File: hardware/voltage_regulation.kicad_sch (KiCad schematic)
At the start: 33 parts, among them U4 TPS51388VABR, U5 LD39050PU33R

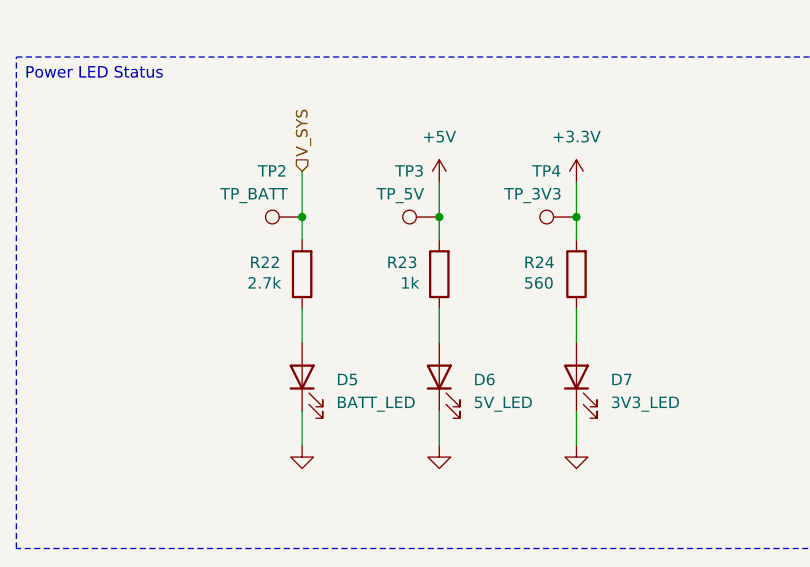
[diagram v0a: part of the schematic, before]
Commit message: Adding MPN to parts
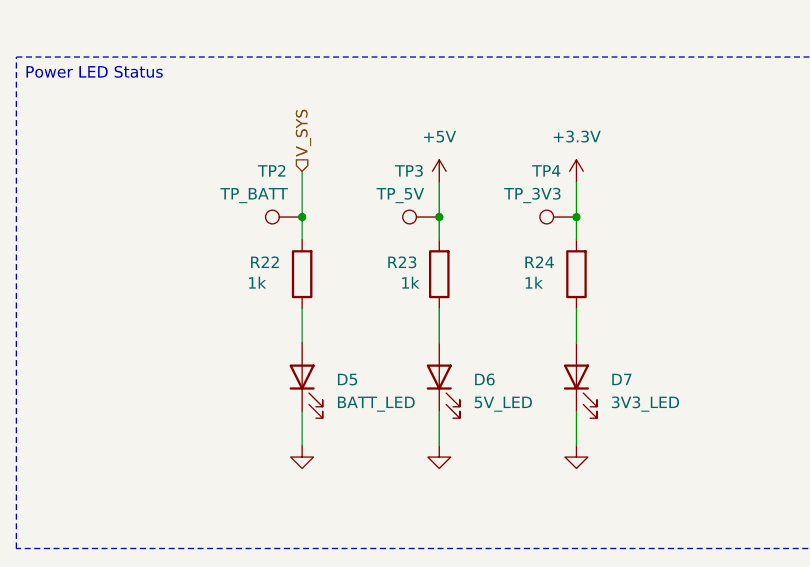
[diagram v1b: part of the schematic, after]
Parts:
- C18, C19: JLCPCB Part# (none) -> C49326357; MPN (none) -> 0603X5R105K160NT
- R15, R19: JLCPCB Part# (none) -> C844916; MPN (none) -> CRCW0603100KFKEA
- R17: JLCPCB Part# (none) -> C844135
- R21: JLCPCB Part# (none) -> C844803; MPN (none) -> CRCW060368K0FKEA
- R22: value 2.7k -> 1k; footprint Resistor_SMD:R_0402_1005Metric -> Resistor_SMD:R_0603_1608Metric; MPN (none) -> CRCW06031K00JNEAC
- R23: footprint Resistor_SMD:R_0402_1005Metric -> Resistor_SMD:R_0603_1608Metric; JLCPCB Part# (none) -> C844135; MPN (none) -> CRCW06031K00JNEAC
- R24: value 560 -> 1k; footprint Resistor_SMD:R_0402_1005Metric -> Resistor_SMD:R_0603_1608Metric; JLCPCB Part# (none) -> C844135; MPN (none) -> CRCW06031K00JNEAC
- TP2, TP3, TP4: now left out of the parts list

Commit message: Replacing components
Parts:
- C13, C14, C15, C16: JLCPCB Part# C49326685 -> C45783; MPN 0805X5R226M100NT -> CL21A226MAQNNNE
- C18, C19: JLCPCB Part# C49326357 -> C15849; MPN 0603X5R105K160NT -> CL10A105KB8NNNC
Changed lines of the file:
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@@
 			)
 		)
-		(property "MPN" "0805X5R226M100NT"
+		(property "MPN" "CL21A226MAQNNNE"
 			(at 209.55 53.34 0)
 			(hide yes)
@@
 			)
 		)
-		(property "JLCPCB Part#" "C49326685"
+		(property "JLCPCB Part#" "C45783"
 			(at 209.55 53.34 0)
 			(hide yes)
@@
 			)
 		)
-		(property "MPN" "0603X5R105K160NT"
+		(property "MPN" "CL10A105KB8NNNC"
 			(at 177.8 132.08 0)
 			(hide yes)
@@
 			)
 		)
-		(property "JLCPCB Part#" "C49326357"
+		(property "JLCPCB Part#" "C15849"
 			(at 177.8 132.08 0)
 			(hide yes)
@@
 			)
 		)
-		(property "v" ""
-			(at 111.76 139.7 90)
-			(hide yes)
-			(show_name no)
-			(do_not_autoplace no)
-			(effects
-				(font
-					(size 1.27 1.27)
-				)
-			)
-		)
 		(pin "2"
 		)
@@
 			)
 		)
-		(property "v" ""
-			(at 96.52 139.7 90)
-			(hide yes)
-			(show_name no)
-			(do_not_autoplace no)
-			(effects
-				(font
-					(size 1.27 1.27)
-				)
-			)
-		)
 		(pin "2"
 		)
@@
 			)
 		)
-		(property "MPN" "0603X5R105K160NT"
+		(property "MPN" "CL10A105KB8NNNC"
 			(at 223.52 132.08 0)
 			(hide yes)
@@
 			)
 		)
-		(property "JLCPCB Part#" "C49326357"
+		(property "JLCPCB Part#" "C15849"
 			(at 223.52 132.08 0)
 			(hide yes)
@@
 			)
 		)
-		(property "MPN" "0805X5R226M100NT"
+		(property "MPN" "CL21A226MAQNNNE"
 			(at 217.17 53.34 0)
 			(hide yes)
@@
 			)
 		)
-		(property "JLCPCB Part#" "C49326685"
+		(property "JLCPCB Part#" "C45783"
 			(at 217.17 53.34 0)
 			(hide yes)
@@
 			)
 		)
-		(property "MPN" "0805X5R226M100NT"
+		(property "MPN" "CL21A226MAQNNNE"
 			(at 232.41 53.34 0)
 			(hide yes)
@@
 			)
 		)
-		(property "JLCPCB Part#" "C49326685"
+		(property "JLCPCB Part#" "C45783"
 			(at 232.41 53.34 0)
 			(hide yes)
@@
 			)
 		)
-		(property "v" ""
-			(at 81.28 139.7 90)
-			(hide yes)
-			(show_name no)
-			(do_not_autoplace no)
-			(effects
-				(font
-					(size 1.27 1.27)
-				)
-			)
-		)
 		(pin "2"
 		)
@@
 			)
 		)
-		(property "MPN" "0805X5R226M100NT"
+		(property "MPN" "CL21A226MAQNNNE"
 			(at 224.79 53.34 0)
 			(hide yes)
@@
 			)
 		)
-		(property "JLCPCB Part#" "C49326685"
+		(property "JLCPCB Part#" "C45783"
 			(at 224.79 53.34 0)
 			(hide yes)

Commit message: Updating schematic
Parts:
- C10, C8, C9: JLCPCB Part # (none) -> C69612; JLCPCB Part# C69612 -> (none)
- C11, C7: JLCPCB Part # (none) -> C1591; JLCPCB Part# C1591 -> (none)
- C12: JLCPCB Part # (none) -> C2167658; JLCPCB Part# C2167658 -> (none)
- C13, C14, C15, C16: JLCPCB Part # (none) -> C45783; JLCPCB Part# C45783 -> (none)
- C17: JLCPCB Part # (none) -> C106211; JLCPCB Part# C106211 -> (none)
- C18, C19: JLCPCB Part # (none) -> C15849; JLCPCB Part# C15849 -> (none)
- D5: JLCPCB Part # (none) -> C5478395; JLCPCB Part# C5478395 -> (none)
- D6: JLCPCB Part # (none) -> C6041957; JLCPCB Part# C6041957 -> (none)
- D7: JLCPCB Part # (none) -> C6650185; JLCPCB Part# C6650185 -> (none)
- L2: JLCPCB Part # (none) -> C5914133; JLCPCB Part# C5914133 -> (none)
- R14, R16: JLCPCB Part # (none) -> C844915; JLCPCB Part# C844915 -> (none)
- R15, R19: JLCPCB Part # (none) -> C844916; JLCPCB Part# C844916 -> (none)
- R17, R23, R24: JLCPCB Part # (none) -> C844135; JLCPCB Part# C844135 -> (none)
- R18: JLCPCB Part # (none) -> C137797; JLCPCB Part# C137797 -> (none)
- R20: JLCPCB Part # (none) -> C137784; JLCPCB Part# C137784 -> (none)
- R21: JLCPCB Part # (none) -> C844803; JLCPCB Part# C844803 -> (none)
- U4: JLCPCB Part # (none) -> C41935536; JLCPCB Part# C41935536 -> (none)
- U5: JLCPCB Part # (none) -> C132827; JLCPCB Part# C132827 -> (none)
